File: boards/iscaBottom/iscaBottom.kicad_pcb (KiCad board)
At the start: 2 copper layers, 178.5 x 157 mm, 39 parts, among them J1 CONN_01X36, J2 CONN_01X36, J3 CONN_01X36

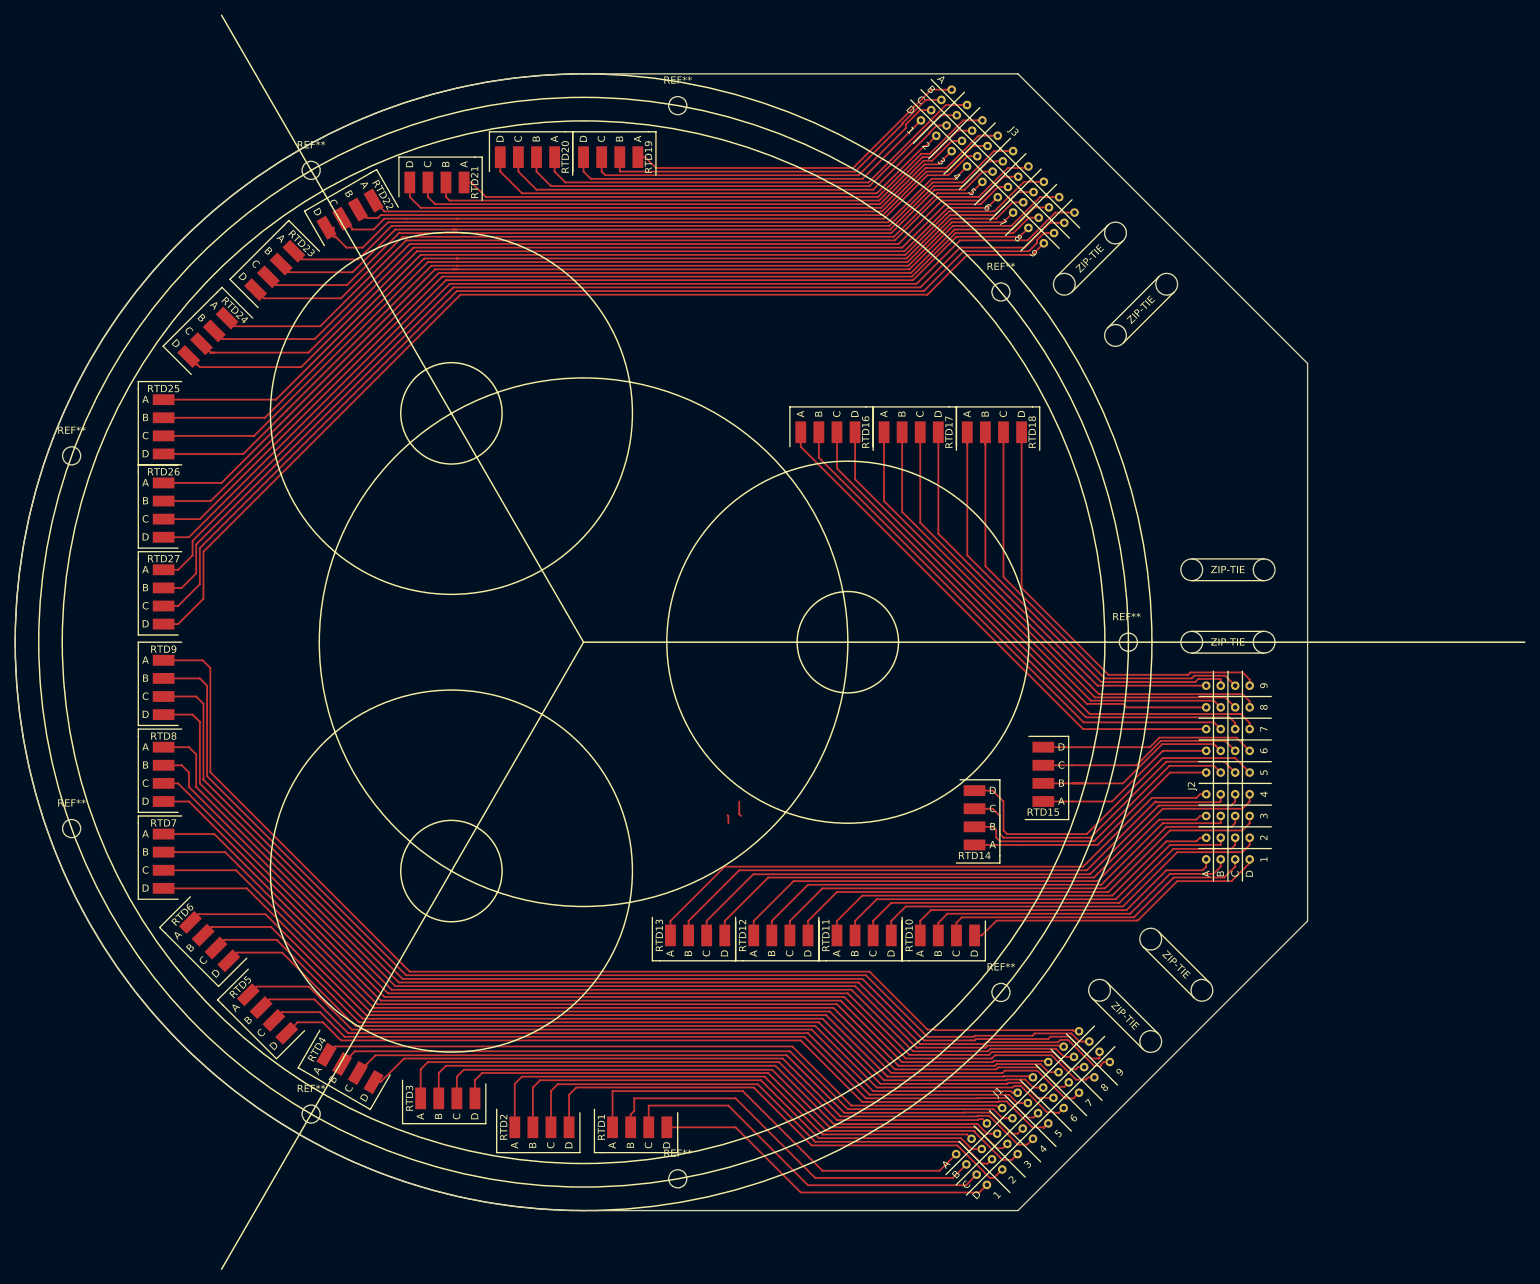
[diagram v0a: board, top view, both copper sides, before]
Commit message: iscaBottom: board comnplete, step exported
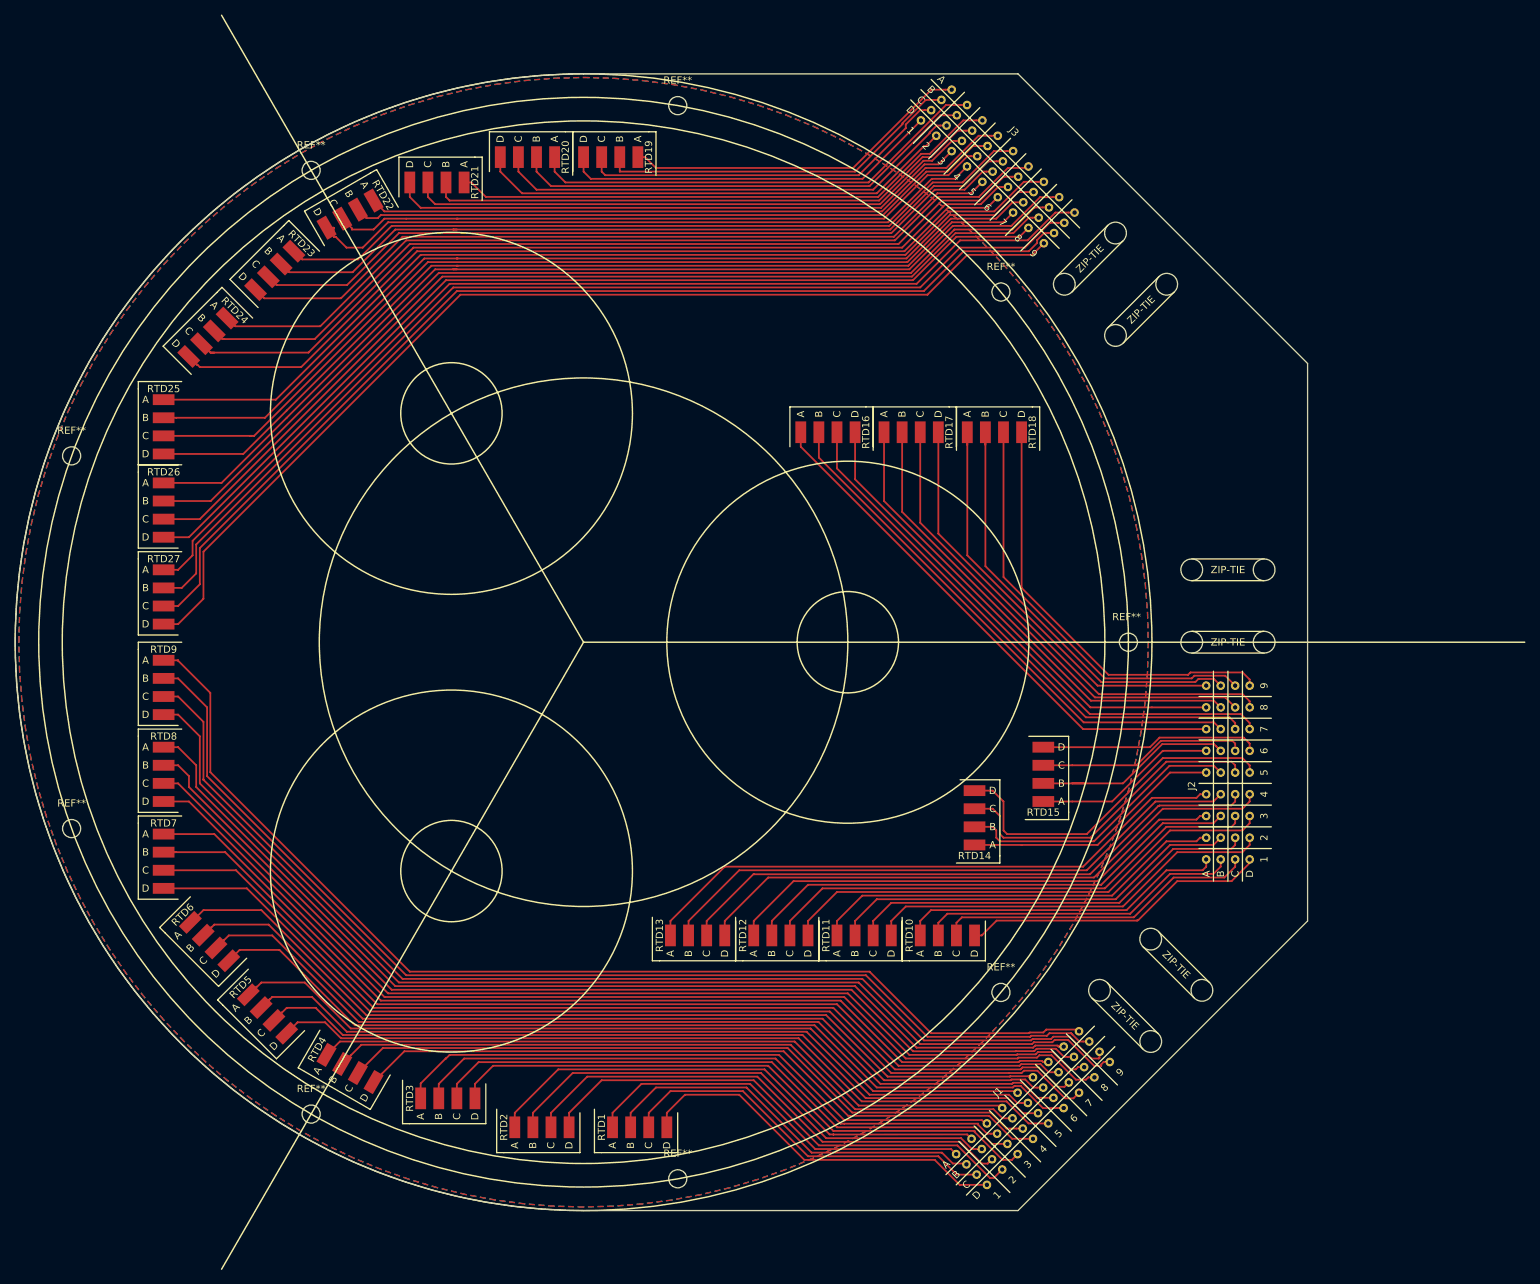
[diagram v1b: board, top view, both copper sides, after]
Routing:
- net Net-(J1-Pad4): track 48.4 -> 52.4 mm
- net (no net): track 3.27 -> 0.00 mm
- net Net-(J1-Pad1): track 58.0 -> 55.1 mm
- net Net-(J1-Pad23): track 125.3 -> 127.4 mm
- net Net-(J1-Pad17): track 112.8 -> 114.9 mm
- net Net-(J1-Pad22): track 125.8 -> 127.6 mm
- net Net-(J1-Pad18): track 112.3 -> 114.2 mm
- net Net-(J1-Pad33): track 156.1 -> 154.5 mm
- net Net-(J1-Pad19): track 112.3 -> 113.9 mm
- net Net-(J1-Pad34): track 156.3 -> 154.8 mm
- net Net-(J1-Pad5): track 73.1 -> 71.6 mm
- net Net-(J1-Pad35): track 157.5 -> 156.0 mm
- net Net-(J1-Pad6): track 71.8 -> 70.6 mm
- net Net-(J1-Pad2): track 55.4 -> 54.2 mm
- net Net-(J1-Pad36): track 156.5 -> 155.4 mm
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- added copper zone on B.Cu, net (none)
- added copper zone on F.Cu, net (none)

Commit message: iscaBottom: v2 electricly complete
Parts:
- RTD15: footprint footprints:4wire_SMDsolder -> footprints:4wire_SMDsolder_reverse
- moved RTD10 77.3 mm to (203.5, 63.5), turned to 270 degrees
- moved RTD11 77.3 mm to (192.0, 63.5), turned to 270 degrees
- moved RTD12 77.3 mm to (180.5, 63.5), turned to 270 degrees
- moved RTD13 77.3 mm to (169.0, 63.5), turned to 270 degrees
- moved RTD16 66.9 mm to (174.0, 136.5), turned to 90 degrees
- moved RTD17 66.9 mm to (185.5, 136.5), turned to 90 degrees
- moved RTD18 66.9 mm to (197.0, 136.5), turned to 90 degrees
- moved J2 65.6 mm to (239.5, 64.5), turned to 270 degrees
- moved RTD15 53.0 mm to (162.5, 136.5), turned to 90 degrees
- moved RTD14 45.0 mm to (210.5, 83.5)
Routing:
- net Net-(J2-Pad21): track 25.4 -> 106.7 mm
- net Net-(J2-Pad23): track 29.1 -> 107.6 mm
- net Net-(J2-Pad22): track 28.9 -> 107.1 mm
- net Net-(J2-Pad24): track 30.4 -> 108.1 mm
- net Net-(J2-Pad20): track 48.6 -> 23.2 mm
- net Net-(J2-Pad26): track 74.5 -> 94.3 mm
- net Net-(J2-Pad25): track 74.2 -> 93.8 mm
- net Net-(J2-Pad28): track 75.8 -> 95.3 mm
- net Net-(J2-Pad27): track 75.4 -> 94.8 mm
- net Net-(J2-Pad19): track 44.7 -> 25.8 mm
- net Net-(J2-Pad31): track 66.6 -> 82.1 mm
- net Net-(J2-Pad30): track 66.2 -> 81.6 mm
- net Net-(J2-Pad29): track 65.8 -> 81.1 mm
- net Net-(J2-Pad32): track 67.4 -> 82.6 mm
- net Net-(J2-Pad18): track 40.1 -> 28.9 mm
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
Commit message: iscaBottom: board_completed
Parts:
- added B: MountingHole_2.5mm, Mounting_Holes:MountingHole_2.5mm, F.Cu at (230.0, 121.4)
- added C: MountingHole_2.5mm, Mounting_Holes:MountingHole_2.5mm, F.Cu at (236.0, 117.5)
- added G***: LOGO, footprints:LOGO_Viper_116mm_34mm_inverted, B.Cu at (155.0, 95.0)
- added R1: 0, Resistors_SMD:R_0603_HandSoldering, F.Cu at (156.1, 175.0)
- added REF**: MountingHole_2.5mm_Pad_Via, Mounting_Holes:MountingHole_2.5mm_Pad_Via, F.Cu at (225.0, 100.0)
- A: renamed from REF**; value MountingHole_2.5mm -> MountingHole_2.5mm_Pad_Via
- REF** (x8): value MountingHole_2.5mm -> MountingHole_2.5mm_Pad_Via; footprint Mounting_Holes:MountingHole_2.5mm -> Mounting_Holes:MountingHole_2.5mm_Pad_Via
- moved A 27.8 mm to (236.0, 125.5)
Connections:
- REF** pad 1: (no net) -> /shield (x8)
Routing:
- added copper zone on F.Cu, net /shield
- removed copper zone on F.Cu, net (none)
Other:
- board text added: "REXUS-Viper ISCA Bottom PCB ©rchojetzki"
